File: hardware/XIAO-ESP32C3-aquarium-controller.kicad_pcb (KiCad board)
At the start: 2 copper layers, 72 x 99 mm, 43 parts, among them J1 Conn_01x02, J2 Conn_01x07, J3 Conn_01x06, J4 Conn_01x03, J5 Conn_01x03, K1 SANYOU_SRD_Form_C, K2 SANYOU_SRD_Form_C, K3 SANYOU_SRD_Form_C, Q1 AO3400A, Q2 AO3400A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

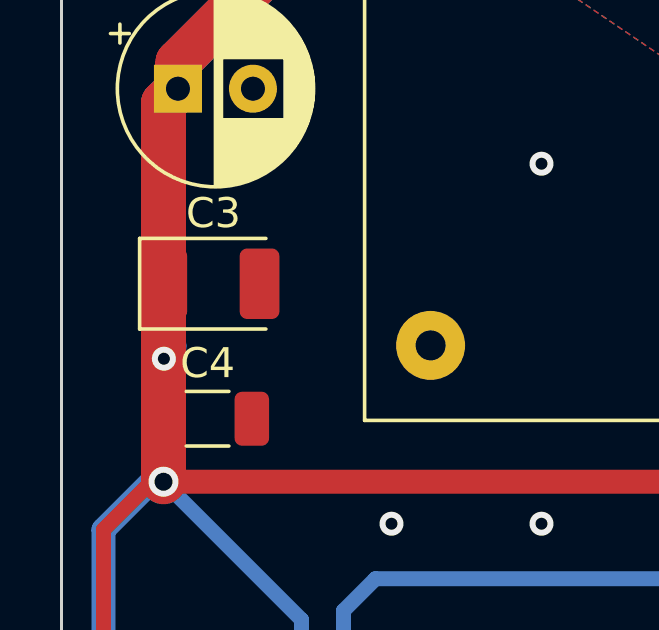
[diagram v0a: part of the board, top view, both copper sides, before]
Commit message: change tantalum capacitor to ceramic
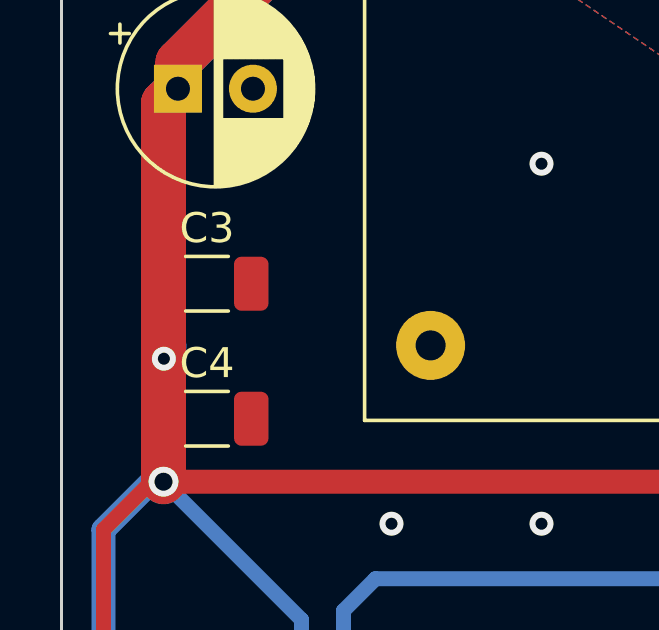
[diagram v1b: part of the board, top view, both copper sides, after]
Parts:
- C3: value 100uF -> 47uF; footprint Capacitor_Tantalum_SMD:CP_EIA-3528-21_Kemet-B -> Capacitor_SMD:C_1206_3216Metric
- moved C3 0.21 mm to (35.5, 51.0)
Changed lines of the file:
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@@
   )
   (footprint "Capacitor_SMD:C_1206_3216Metric" (layer "F.Cu")
-    (at 35.469 55.5)
+    (at 35.45 55.5)
     (descr "Capacitor SMD 1206 (3216 Metric), square (rectangular) end terminal, IPC_7351 nominal, (Body size source: IPC-SM-782 page 76, https://www.pcb-3d.com/wordpress/wp-content/uploads/ipc-sm-782a_amendment_1_and_2.pdf), generated with kicad-footprint-generator")
     (tags "capacitor")
@@
     )
   )
-  (footprint "Capacitor_Tantalum_SMD:CP_EIA-3528-21_Kemet-B" (layer "F.Cu")
-    (at 35.664 51)
-    (descr "Tantalum Capacitor SMD Kemet-B (3528-21 Metric), IPC_7351 nominal, (Body size from: http://www.kemet.com/Lists/ProductCatalog/Attachments/253/KEM_TC101_STD.pdf), generated with kicad-footprint-generator")
-    (tags "capacitor tantalum")
-    (property "JLCPCB Part #" "C16133")
+  (footprint "Capacitor_SMD:C_1206_3216Metric" (layer "F.Cu")
+    (at 35.45 51)
+    (descr "Capacitor SMD 1206 (3216 Metric), square (rectangular) end terminal, IPC_7351 nominal, (Body size source: IPC-SM-782 page 76, https://www.pcb-3d.com/wordpress/wp-content/uploads/ipc-sm-782a_amendment_1_and_2.pdf), generated with kicad-footprint-generator")
+    (tags "capacitor")
+    (property "JLCPCB Part #" "C96123")
     (property "Sheetfile" "AC-DC.kicad_sch")
     (property "Sheetname" "AC-DC")
@@
     (property "ki_keywords" "cap capacitor")
     (attr smd)
-    (fp_text reference "C3" (at 0 -2.35) (layer "F.SilkS")
-        (effects (font (size 1 1) (thickness 0.15)))
-    )
-    (fp_text value "100uF" (at 0 2.35) (layer "F.Fab")
+    (fp_text reference "C3" (at 0 -1.85) (layer "F.SilkS")
+        (effects (font (size 1 1) (thickness 0.15)))
+    )
+    (fp_text value "47uF" (at 0 1.85) (layer "F.Fab")
         (effects (font (size 1 1) (thickness 0.15)))
     )
     (fp_text user "${REFERENCE}" (at 0 0) (layer "F.Fab")
-        (effects (font (size 0.88 0.88) (thickness 0.13)))
-    )
-    (fp_line (start -2.46 -1.51) (end -2.46 1.51)
-      (stroke (width 0.12) (type solid)) (layer "F.SilkS"))
-    (fp_line (start -2.46 1.51) (end 1.75 1.51)
-      (stroke (width 0.12) (type solid)) (layer "F.SilkS"))
-    (fp_line (start 1.75 -1.51) (end -2.46 -1.51)
-      (stroke (width 0.12) (type solid)) (layer "F.SilkS"))
-    (fp_line (start -2.45 -1.65) (end 2.45 -1.65)
-      (stroke (width 0.05) (type solid)) (layer "F.CrtYd"))
-    (fp_line (start -2.45 1.65) (end -2.45 -1.65)
-      (stroke (width 0.05) (type solid)) (layer "F.CrtYd"))
-    (fp_line (start 2.45 -1.65) (end 2.45 1.65)
-      (stroke (width 0.05) (type solid)) (layer "F.CrtYd"))
-    (fp_line (start 2.45 1.65) (end -2.45 1.65)
-      (stroke (width 0.05) (type solid)) (layer "F.CrtYd"))
-    (fp_line (start -1.75 -0.7) (end -1.75 1.4)
-      (stroke (width 0.1) (type solid)) (layer "F.Fab"))
-    (fp_line (start -1.75 1.4) (end 1.75 1.4)
-      (stroke (width 0.1) (type solid)) (layer "F.Fab"))
-    (fp_line (start -1.05 -1.4) (end -1.75 -0.7)
-      (stroke (width 0.1) (type solid)) (layer "F.Fab"))
-    (fp_line (start 1.75 -1.4) (end -1.05 -1.4)
-      (stroke (width 0.1) (type solid)) (layer "F.Fab"))
-    (fp_line (start 1.75 1.4) (end 1.75 -1.4)
-      (stroke (width 0.1) (type solid)) (layer "F.Fab"))
-    (pad "1" smd roundrect (at -1.5375 0) (size 1.325 2.35) (layers "F.Cu" "F.Paste" "F.Mask") (roundrect_rratio 0.1886792453)
+        (effects (font (size 0.8 0.8) (thickness 0.12)))
+    )
+    (fp_line (start -0.711252 -0.91) (end 0.711252 -0.91)
+      (stroke (width 0.12) (type solid)) (layer "F.SilkS"))
+    (fp_line (start -0.711252 0.91) (end 0.711252 0.91)
+      (stroke (width 0.12) (type solid)) (layer "F.SilkS"))
+    (fp_line (start -2.3 -1.15) (end 2.3 -1.15)
+      (stroke (width 0.05) (type solid)) (layer "F.CrtYd"))
+    (fp_line (start -2.3 1.15) (end -2.3 -1.15)
+      (stroke (width 0.05) (type solid)) (layer "F.CrtYd"))
+    (fp_line (start 2.3 -1.15) (end 2.3 1.15)
+      (stroke (width 0.05) (type solid)) (layer "F.CrtYd"))
+    (fp_line (start 2.3 1.15) (end -2.3 1.15)
+      (stroke (width 0.05) (type solid)) (layer "F.CrtYd"))
+    (fp_line (start -1.6 -0.8) (end 1.6 -0.8)
+      (stroke (width 0.1) (type solid)) (layer "F.Fab"))
+    (fp_line (start -1.6 0.8) (end -1.6 -0.8)
+      (stroke (width 0.1) (type solid)) (layer "F.Fab"))
+    (fp_line (start 1.6 -0.8) (end 1.6 0.8)
+      (stroke (width 0.1) (type solid)) (layer "F.Fab"))
+    (fp_line (start 1.6 0.8) (end -1.6 0.8)
+      (stroke (width 0.1) (type solid)) (layer "F.Fab"))
+    (pad "1" smd roundrect (at -1.475 0) (size 1.15 1.8) (layers "F.Cu" "F.Paste" "F.Mask") (roundrect_rratio 0.217391)
       (net 1 "+5V") (pintype "passive"))
-    (pad "2" smd roundrect (at 1.5375 0) (size 1.325 2.35) (layers "F.Cu" "F.Paste" "F.Mask") (roundrect_rratio 0.1886792453)
+    (pad "2" smd roundrect (at 1.475 0) (size 1.15 1.8) (layers "F.Cu" "F.Paste" "F.Mask") (roundrect_rratio 0.217391)
       (net 2 "GND") (pintype "passive"))
-    (model "${KICAD6_3DMODEL_DIR}/Capacitor_Tantalum_SMD.3dshapes/CP_EIA-3528-21_Kemet-B.wrl"
-      (offset (xyz 0 0 0))
-      (scale (xyz 1 1 1))
+    (model "${KICAD6_3DMODEL_DIR}/Capacitor_SMD.3dshapes/C_1206_3216Metric.wrl"
+      (offset (xyz 0 0 0))
+      (scale (xyz 1 1 1))

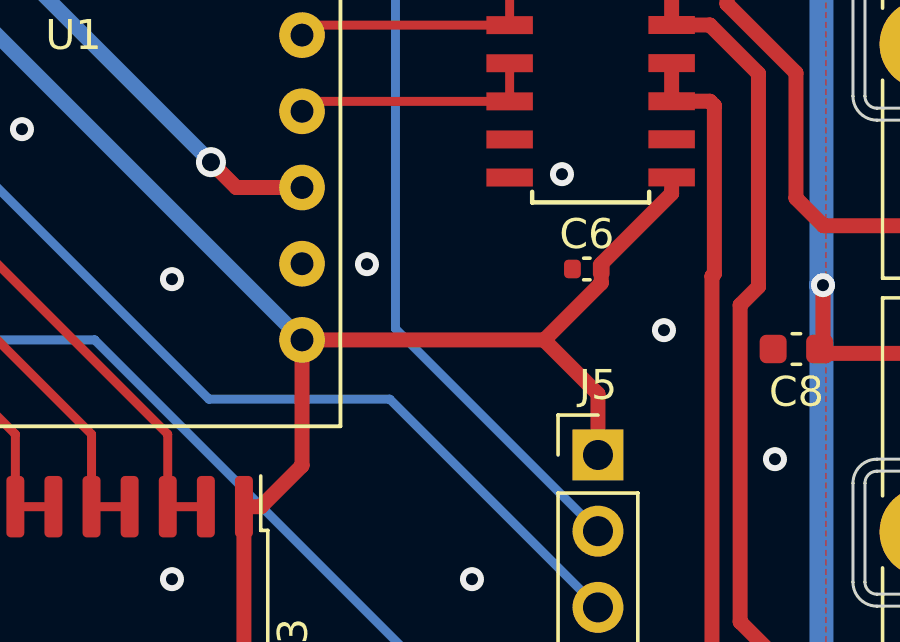
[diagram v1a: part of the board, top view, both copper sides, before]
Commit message: 3v3 instead 5v on connector
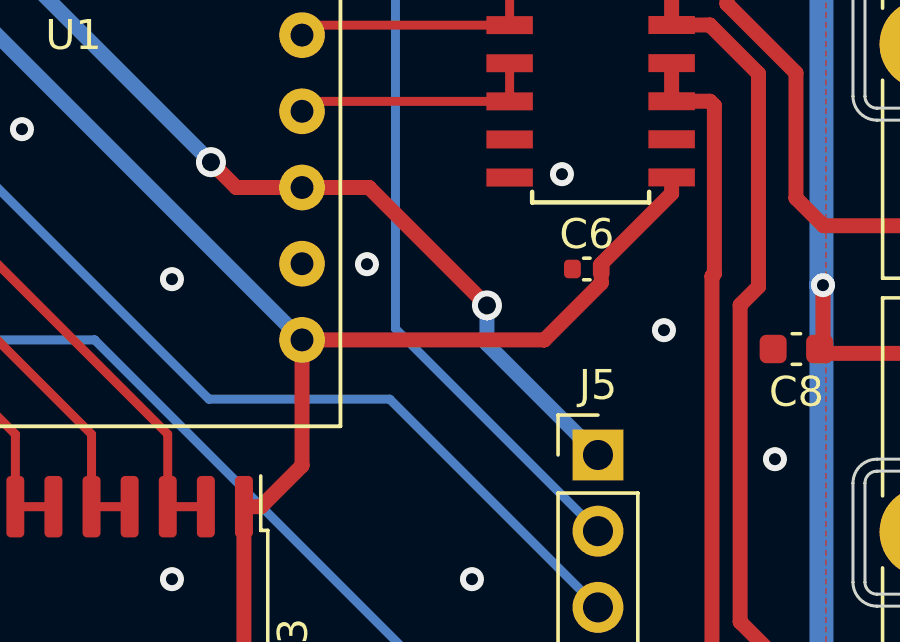
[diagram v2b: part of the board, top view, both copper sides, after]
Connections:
- J5 pad 1: +5V -> +3.3V
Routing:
- net +3.3V: track 45.8 -> 60.2 mm, vias 1 -> 2
- net +5V: track 507.3 -> 502.7 mm
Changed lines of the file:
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@@
       (stroke (width 0.1) (type solid)) (layer "F.Fab"))
     (pad "1" thru_hole rect (at 0 0) (size 1.7 1.7) (drill 1) (layers "*.Cu" "*.Mask")
-      (net 1 "+5V") (pinfunction "Pin_1") (pintype "passive"))
+      (net 16 "+3.3V") (pinfunction "Pin_1") (pintype "passive"))
     (pad "2" thru_hole oval (at 0 2.54) (size 1.7 1.7) (drill 1) (layers "*.Cu" "*.Mask")
       (net 35 "/D7") (pinfunction "Pin_2") (pintype "passive"))
@@
   (segment (start 36.4 124.2) (end 46.6 124.2) (width 0.5) (layer "F.Cu") (net 1))
   (segment locked (start 49.9 124.3) (end 56.4 124.3) (width 0.5) (layer "F.Cu") (net 1))
-  (segment (start 60.8 85.8245) (end 59 84.0245) (width 0.5) (layer "F.Cu") (net 1))
   (segment (start 49.12 102.1) (end 49.12 99.005) (width 0.5) (layer "F.Cu") (net 1))
-  (segment (start 60.8 87.86) (end 60.8 85.8245) (width 0.5) (layer "F.Cu") (net 1))
   (segment (start 32 59.2) (end 32 119.8) (width 0.5) (layer "F.Cu") (net 1))
   (segment (start 68.3 84.217) (end 68.189 84.328) (width 0.5) (layer "F.Cu") (net 1))
@@
   (segment (start 50.8 67) (end 57.8 67) (width 0.2) (layer "F.Cu") (net 15))
   (segment (start 35.69575 71.3245) (end 46.4755 71.3245) (width 0.2) (layer "F.Cu") (net 15))
+  (segment (start 53.1695 78.9445) (end 57.1 82.875) (width 0.5) (layer "F.Cu") (net 16))
   (segment (start 52.804 60.833) (end 54.304 59.333) (width 0.5) (layer "F.Cu") (net 16))
   (segment (start 58.461 64.008) (end 58.461 61.41) (width 0.5) (layer "F.Cu") (net 16))
@@
   (segment (start 54.304 59.333) (end 56.384 59.333) (width 0.5) (layer "F.Cu") (net 16))
   (segment (start 48.7445 78.9445) (end 47.9 78.1) (width 0.5) (layer "F.Cu") (net 16))
+  (segment (start 50.93575 78.9445) (end 53.1695 78.9445) (width 0.5) (layer "F.Cu") (net 16))
   (segment (start 56.384 59.333) (end 57.884 60.833) (width 0.5) (layer "F.Cu") (net 16))
   (segment (start 58.461 61.41) (end 57.884 60.833) (width 0.5) (layer "F.Cu") (net 16))
+  (via (at 57.1 82.875) (size 1) (drill 0.6) (layers "F.Cu" "B.Cu") (net 16))
   (via (at 47.9 78.1) (size 1) (drill 0.6) (layers "F.Cu" "B.Cu") (net 16))
   (segment (start 47.9 78.1) (end 40 70.2) (width 0.5) (layer "B.Cu") (net 16))
   (segment (start 41.067 60.833) (end 52.804 60.833) (width 0.5) (layer "B.Cu") (net 16))
+  (segment (start 57.1 82.875) (end 57.1 84.16) (width 0.5) (layer "B.Cu") (net 16))
   (segment (start 40 70.2) (end 40 61.9) (width 0.5) (layer "B.Cu") (net 16))
+  (segment (start 57.1 84.16) (end 60.8 87.86) (width 0.5) (layer "B.Cu") (net 16))
   (segment (start 40 61.9) (end 41.067 60.833) (width 0.5) (layer "B.Cu") (net 16))
   (segment (start 55.425 64) (end 55.344 63.919) (width 0.2) (layer "F.Cu") (net 17))

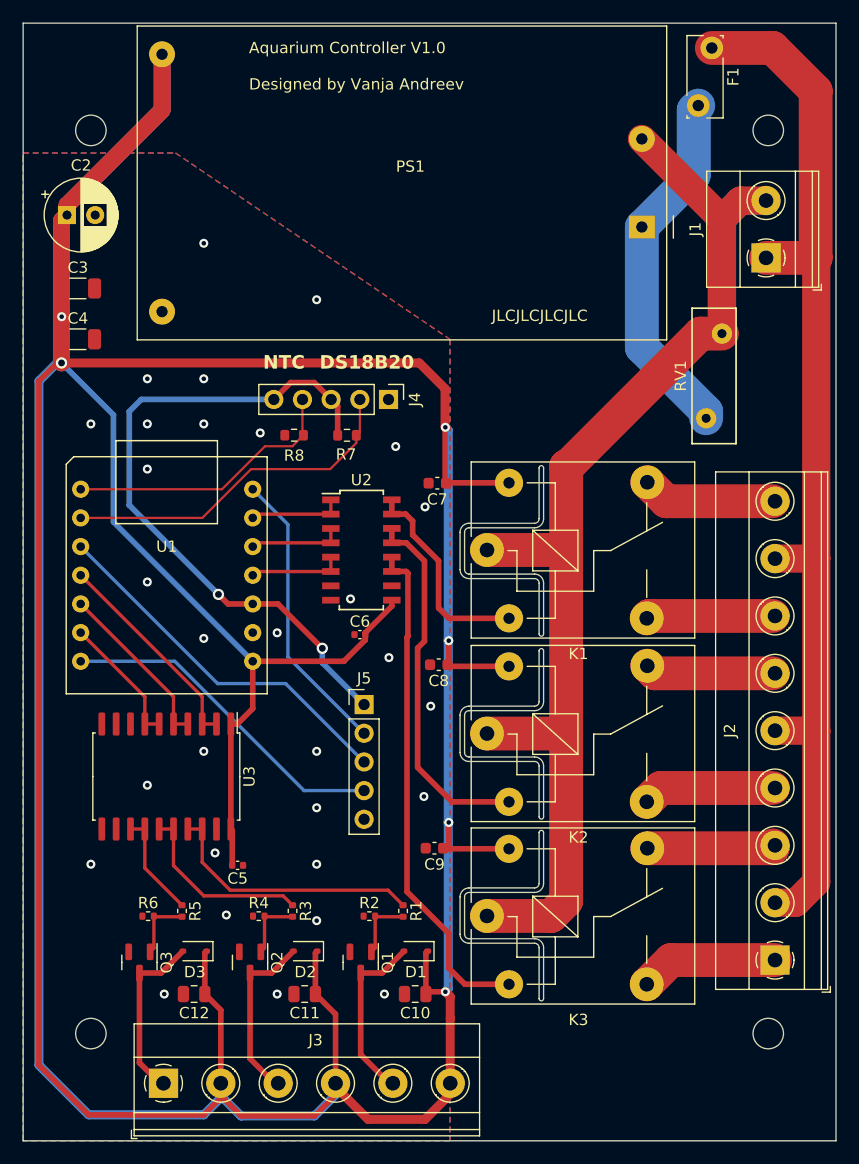
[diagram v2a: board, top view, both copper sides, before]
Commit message: double sided tracks
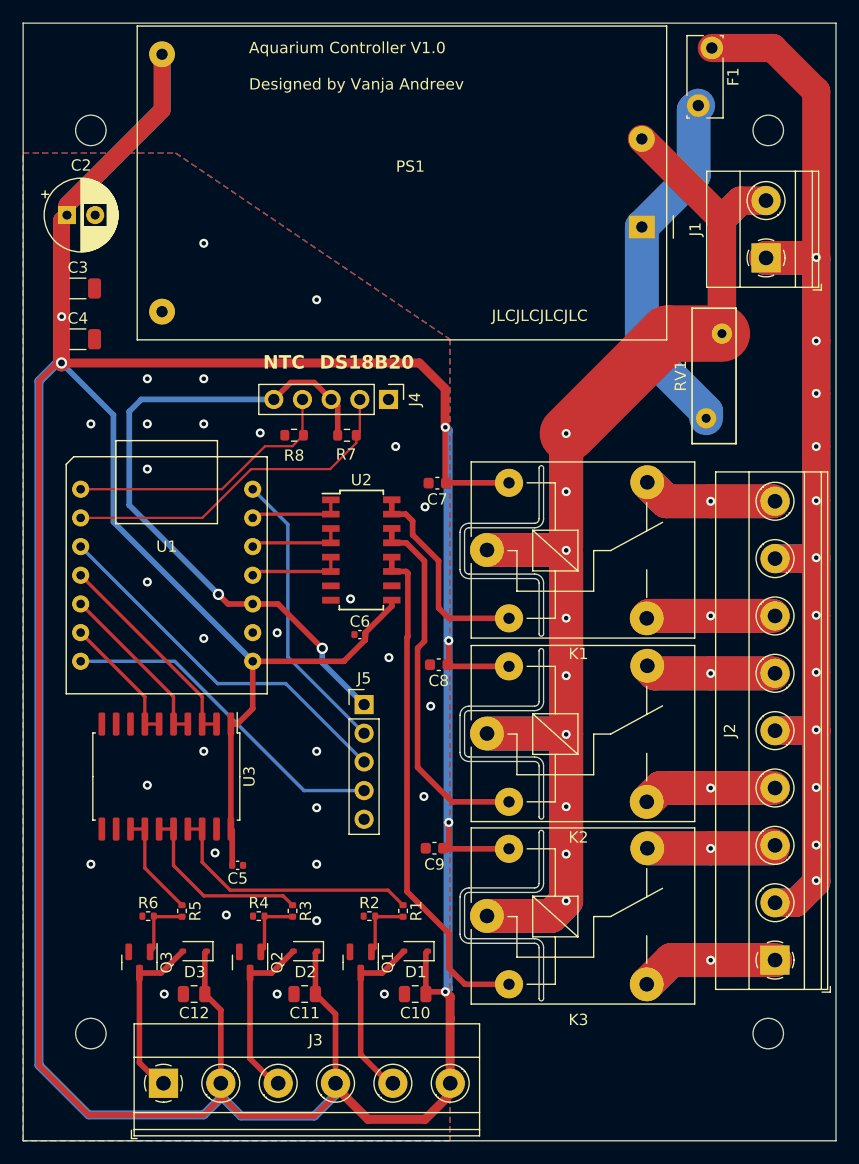
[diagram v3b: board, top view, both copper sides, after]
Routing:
- net AL/L: track 96.9 -> 167.6 mm, vias 0 -> 12
- net AL/N: track 117.1 -> 180.3 mm, vias 0 -> 9
- net /Relay3/NC: track 12.3 -> 24.5 mm, vias 0 -> 1
- net /Relay1/NO: track 11.8 -> 23.6 mm, vias 0 -> 1
- net /Relay2/NC: track 11.7 -> 23.3 mm, vias 0 -> 1
- net /Relay2/NO: track 11.4 -> 22.7 mm, vias 0 -> 1
- net /Relay3/NO: track 11.3 -> 22.3 mm, vias 0 -> 1
- net /Relay1/NC: track 11.2 -> 22.2 mm, vias 0 -> 1
